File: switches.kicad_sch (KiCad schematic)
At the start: 128 parts, among them SW10 SW_Push, SW11 SW_Push, SW14 SW_Push, SW15 SW_Push, SW16 SW_Push, SW18 SW_Push, SW20 SW_Push, SW21 SW_Push, SW22 SW_Push, SW23 SW_Push, SW24 SW_Push, SW25 SW_Push, SW26 SW_Push, SW27 SW_Push, SW28 SW_Push, SW29 SW_Push, SW3 SW_Push, SW30 SW_Push, SW31 SW_Push, SW32 SW_Push, SW35 SW_Push, SW36 SW_Push, SW37 SW_Push, SW38 SW_Push, SW39 SW_Push, SW40 SW_Push, SW41 SW_Push, SW42 SW_Push, SW43 SW_Push, SW44 SW_Push, SW45 SW_Push, SW46 SW_Push, SW47 SW_Push, SW48 SW_Push, SW49 SW_Push, SW5 SW_Push, SW50 SW_Push, SW51 SW_Push, SW52 SW_Push, SW53 SW_Push, SW54 SW_Push, SW56 SW_Push, SW58 SW_Push, SW59 SW_Push, SW60 SW_Push, SW61 SW_Push, SW62 SW_Push, SW65 SW_Push, SW66 SW_Push, SW67 SW_Push, SW68 SW_Push, SW69 SW_Push, SW7 SW_Push, SW71 SW_Push, SW73 SW_Push, SW74 SW_Push, SW75 SW_Push, SW76 SW_Push, SW78 SW_Push, SW79 SW_Push, SW80 SW_Push, SW82 SW_Push, SW84 SW_Push, SW86 SW_Push, SW9 SW_Push

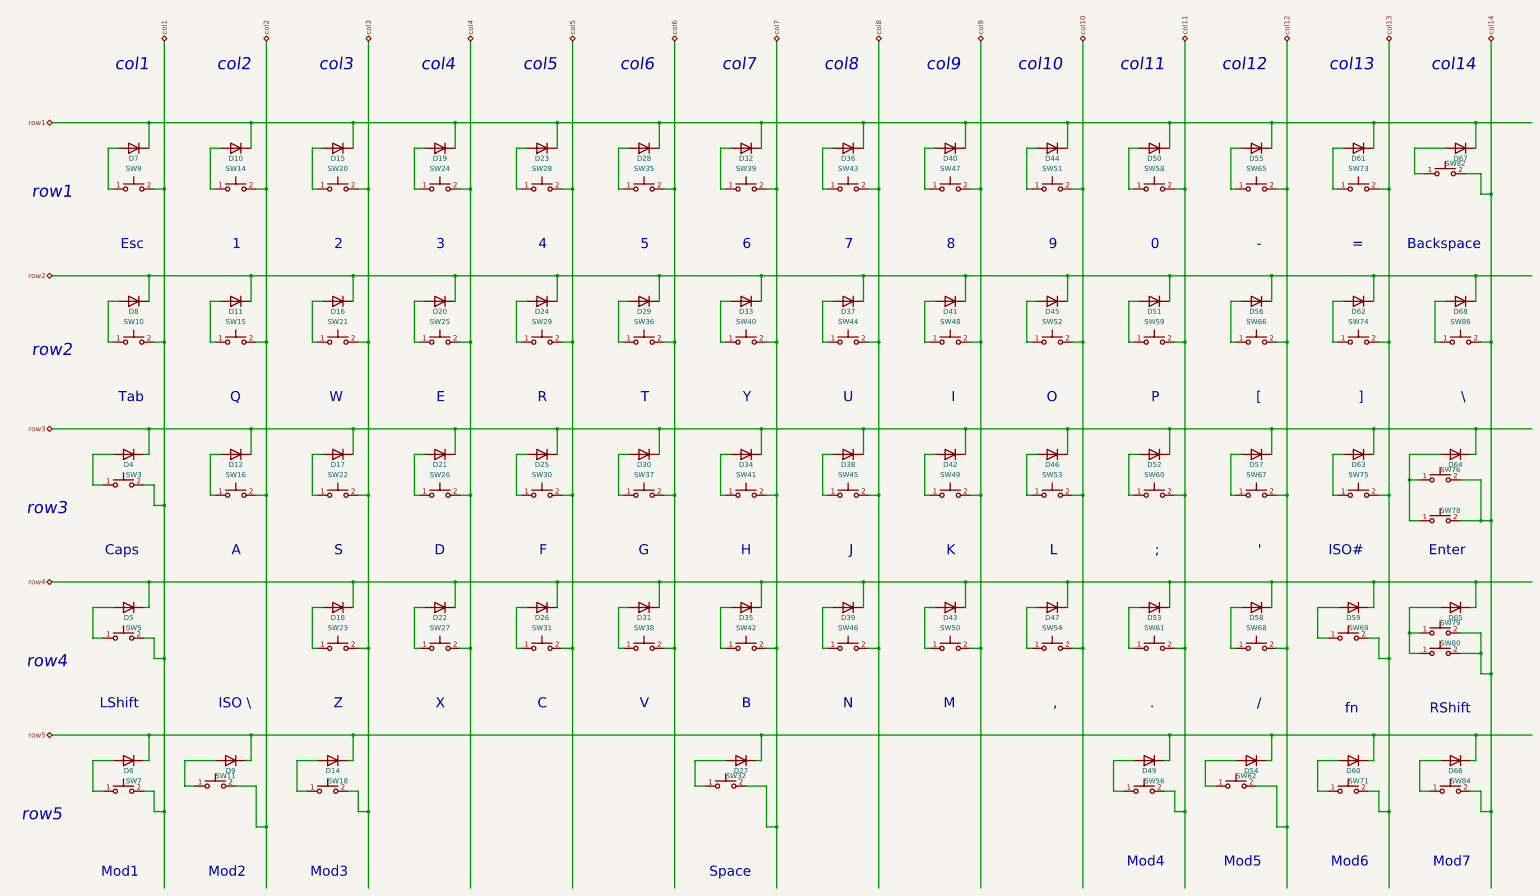
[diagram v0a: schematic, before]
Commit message: change keymap to jy60
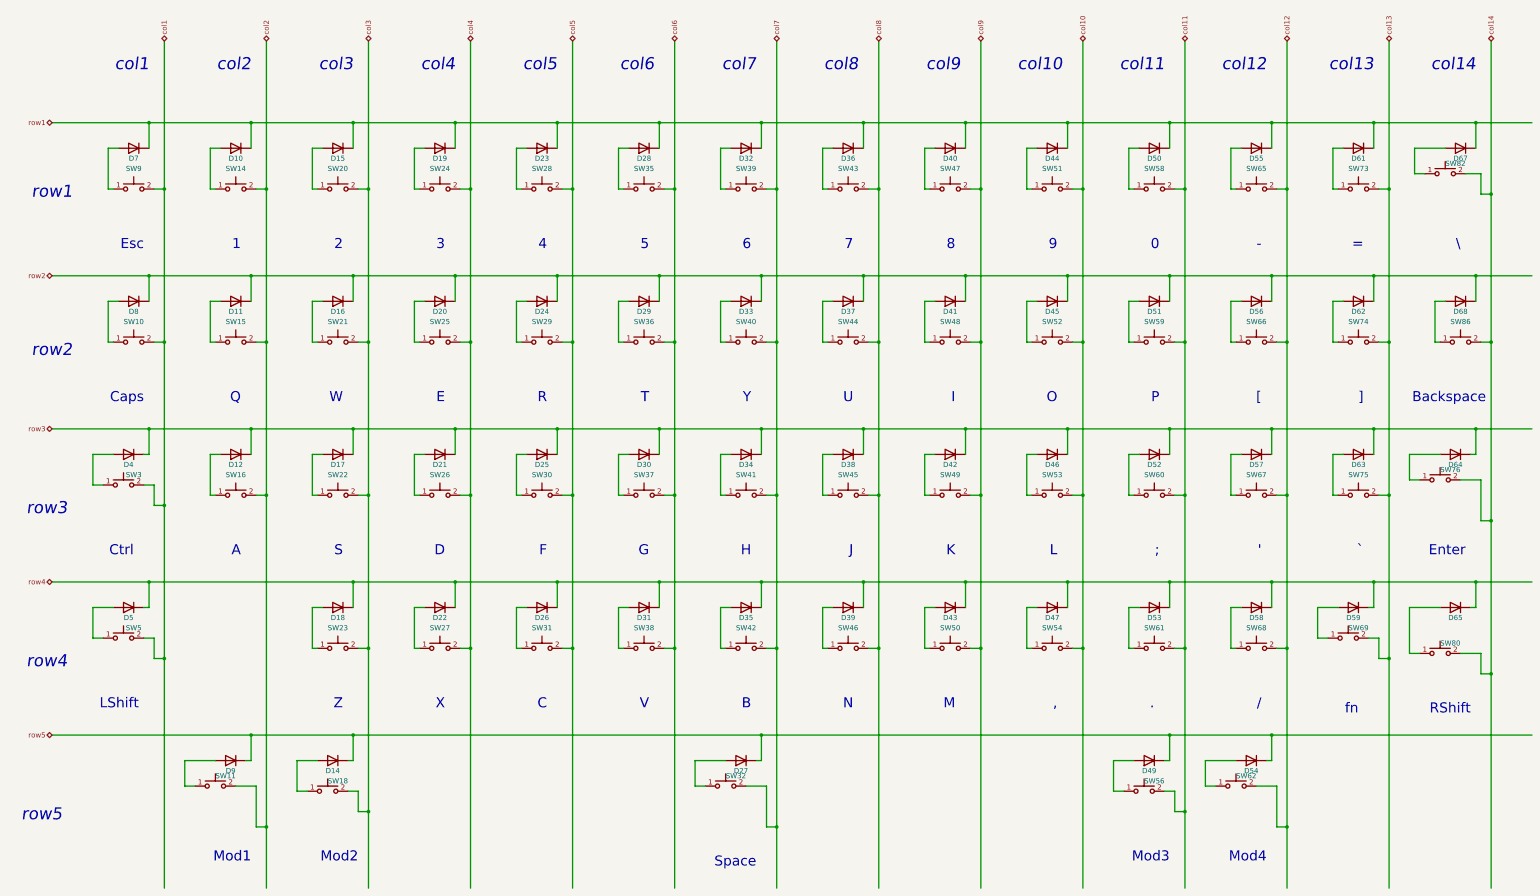
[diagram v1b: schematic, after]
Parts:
- removed D6, D60, D66: 1N4148, Diode_SMD:D_0805_2012Metric, symbol Diode:1N4148
- removed SW7, SW71, SW78, SW79, SW84: SW_Push, keyswitches:Kailh_socket_MX, symbol Switch:SW_Push
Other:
- note added: "Ctrl"
- note added: "`"
- note removed: "ISO \"
- note removed: "ISO#"
- note removed: "Mod5"
- note removed: "Mod6"
- note removed: "Mod7"
- note removed: "Tab"
